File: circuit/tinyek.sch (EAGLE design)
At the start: 13 parts, among them IC1 ATTiny13A, Q1 2N7000

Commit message: update
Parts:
- C1, C2: device resistor:C-EU050-024X044 -> c-j:C-50V-0302-5.08
- R1: device resistor:R-US_0207/7 -> r-j:R-1/4W-07.62
- R3, R4: device resistor:R-US_0204/7 -> r-j:R-1/4W-07.62
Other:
- moved on the sheet: G1, INPUT, KEY-

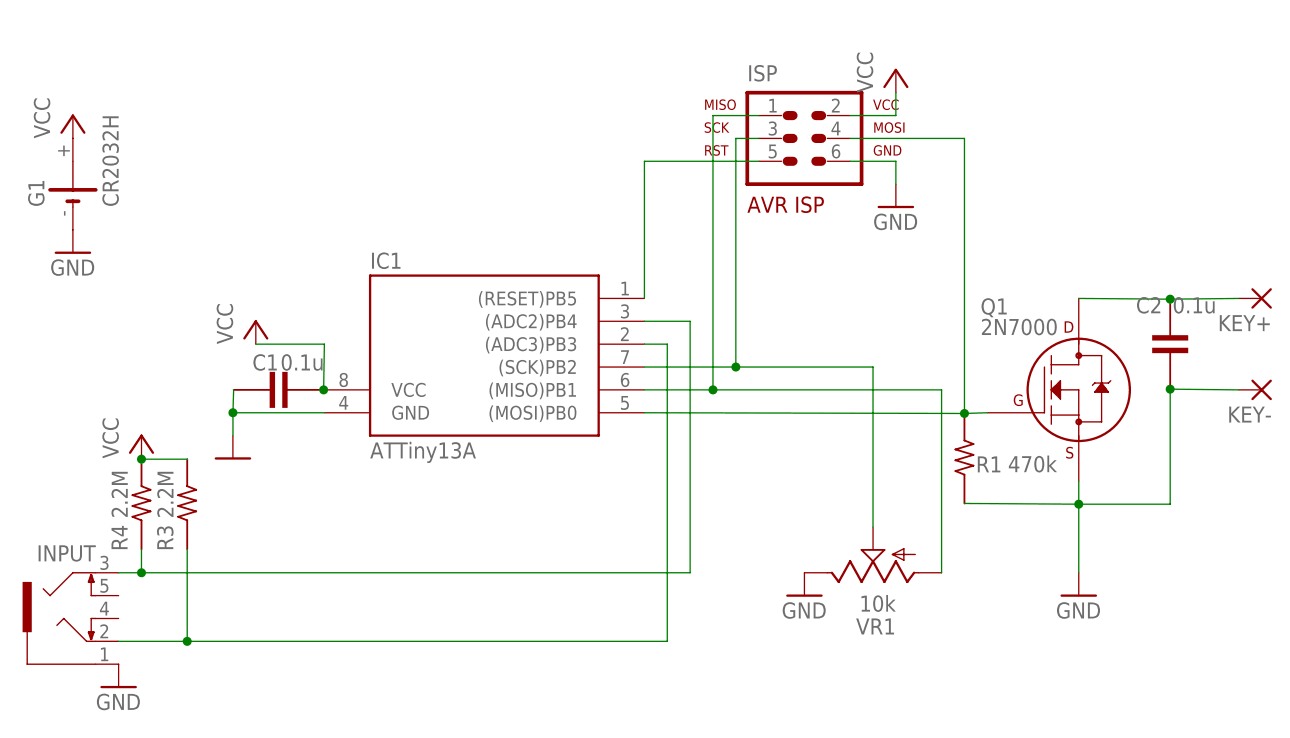
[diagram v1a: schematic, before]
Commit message: ピンによってドライブ能力が違うので、一応余裕がある配置に設計変更。ほんと意味はないと思う
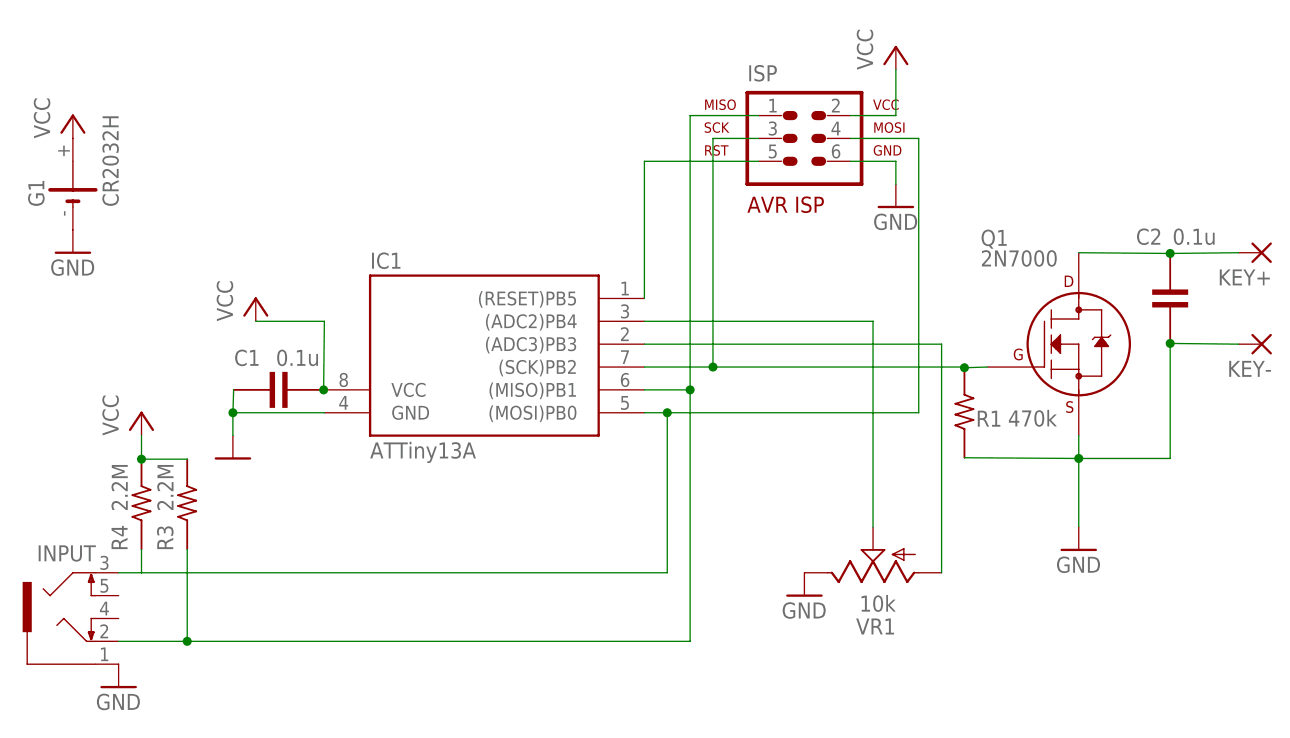
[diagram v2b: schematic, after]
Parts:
- R1: device r-j:R-1/4W-07.62 -> r-j:R-1/4W-02.54-V
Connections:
- removed net N$7: IC1.(ADC2)PB4, INPUT.3, R4.2
- new net N$10: IC1.(MOSI)PB0, INPUT.3, ISP.4, R4.2
- net N$4: now also IC1.(SCK)PB2, ISP.3; no longer IC1.(MOSI)PB0, ISP.4
- net N$5: now also IC1.(ADC3)PB3; no longer IC1.(MISO)PB1, ISP.1
- net N$6: now also IC1.(ADC2)PB4; no longer IC1.(SCK)PB2, ISP.3
- net N$8: now also IC1.(MISO)PB1, ISP.1; no longer IC1.(ADC3)PB3
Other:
- moved on the sheet: C2, KEY+, KEY-, Q1, R1
